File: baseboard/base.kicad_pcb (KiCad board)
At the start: 2 copper layers, 180 x 45 mm, 41 parts, among them J1 Conn_02x05_Odd_Even, J2 Barrel_Jack, J3 Barrel_Jack, J4 Conn_01x03_Male, Q1 BSS138, Q2 BSS138, Q3 BSS138, Q4 BSS138, Q5 BSS138, SW1 SW_Push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

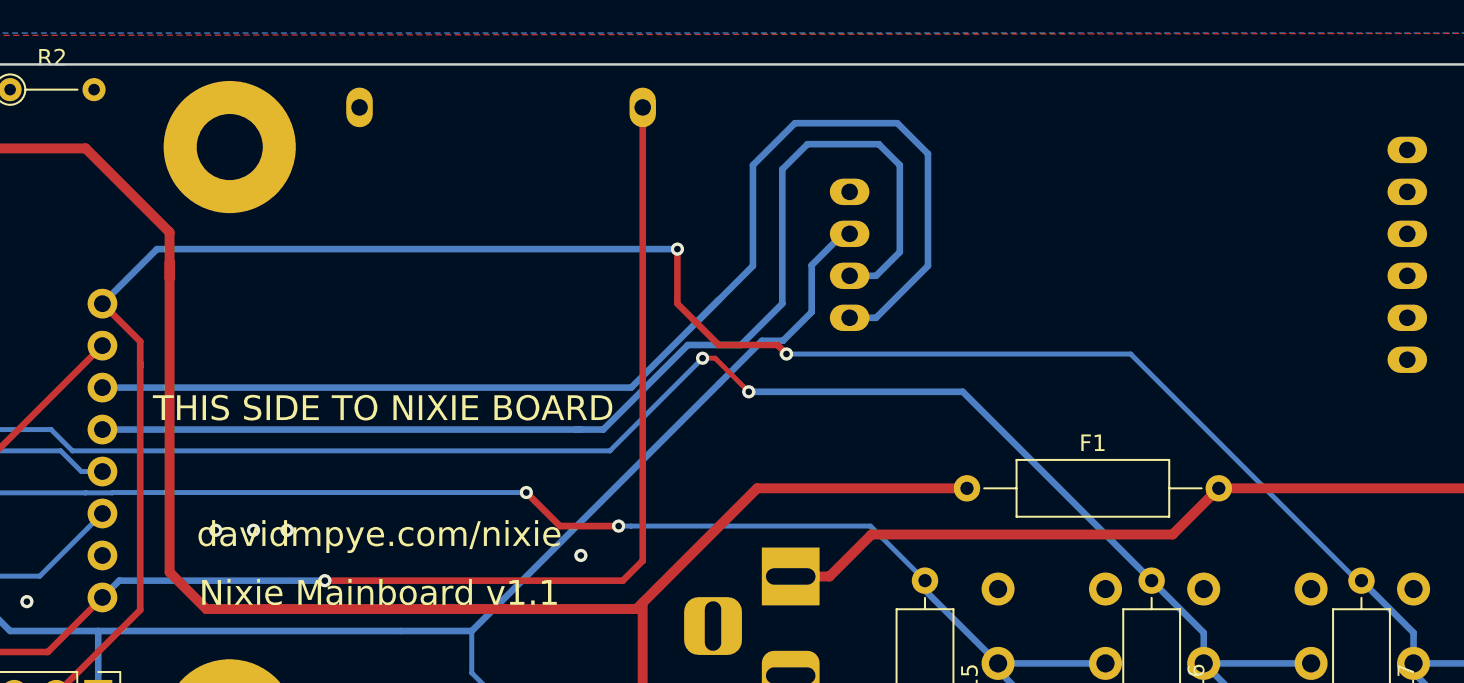
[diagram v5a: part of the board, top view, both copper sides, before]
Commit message: Track rerouting/tidying
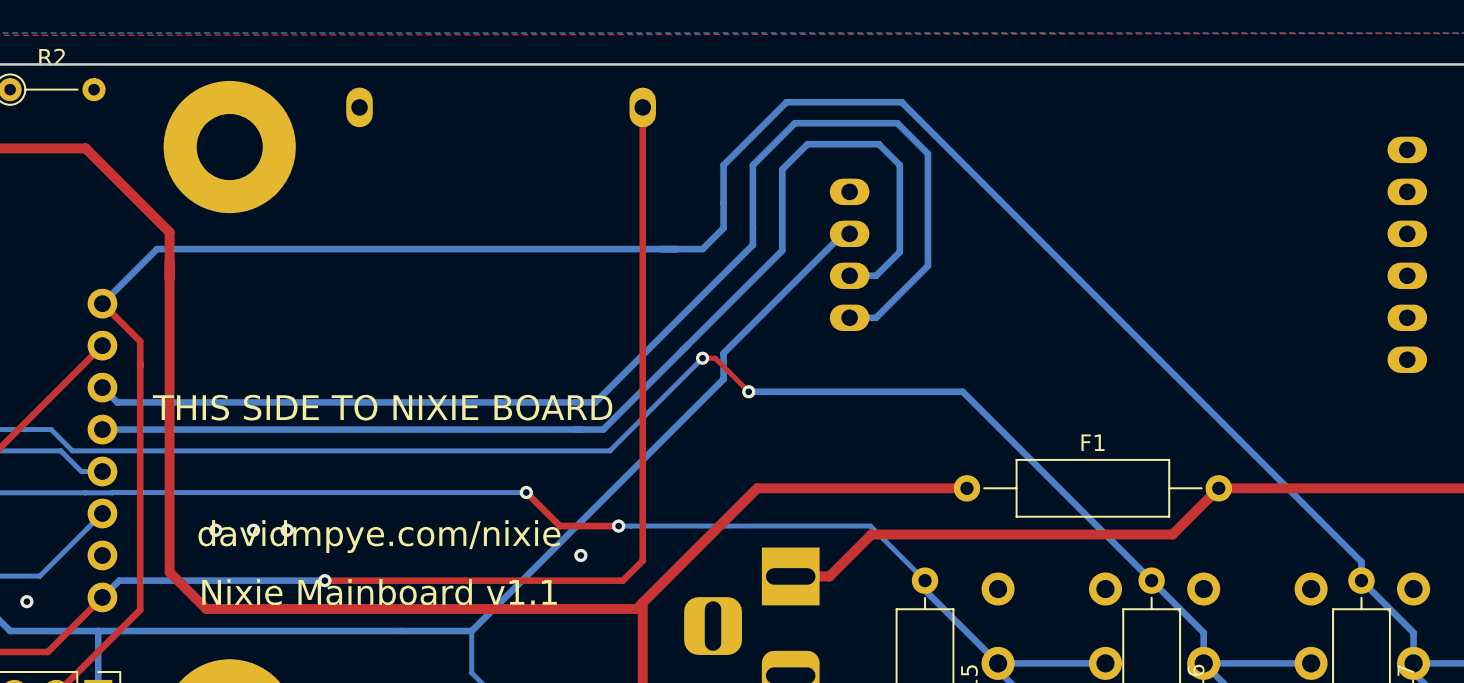
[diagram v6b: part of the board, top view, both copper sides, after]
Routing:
- net SW_3: track 137.6 -> 146.9 mm, vias 2 -> 0
- net SCL: track 75.7 -> 73.8 mm
- net SDA: track 69.8 -> 68.4 mm
- net +3V3: track 245.9 -> 245.1 mm
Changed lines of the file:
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@@
     (thickness 1.6)
     (drawings 22)
-    (tracks 367)
+    (tracks 364)
     (zones 0)
     (modules 41)
@@
   )
   (setup
-    (last_trace_width 0.25)
+    (last_trace_width 0.4)
     (user_trace_width 0.3)
     (user_trace_width 0.4)
@@
   (segment (start 101.092 65.532) (end 101.092 64.282) (width 0.4) (layer B.Cu) (net 7))
   (segment (start 123.698 61.722) (end 138.684 46.736) (width 0.4) (layer B.Cu) (net 7))
-  (segment (start 141.262001 44.157999) (end 142.532001 44.157999) (width 0.4) (layer B.Cu) (net 7))
-  (segment (start 138.684 46.736) (end 141.262001 44.157999) (width 0.4) (layer B.Cu) (net 7))
-  (segment (start 142.532001 44.157999) (end 144.272 42.418) (width 0.4) (layer B.Cu) (net 7))
-  (segment (start 144.272 39.581) (end 146.168 37.685) (width 0.4) (layer B.Cu) (net 7))
-  (segment (start 144.272 42.418) (end 144.272 39.581) (width 0.4) (layer B.Cu) (net 7))
-  (segment (start 146.568 37.685) (end 146.168 37.685) (width 0.4) (layer B.Cu) (net 7))
   (segment (start 146.568 37.685) (end 146.168 37.685) (width 0.4) (layer F.Cu) (net 7))
   (segment (start 50.8 70.866) (end 53.086 68.58) (width 0.3) (layer B.Cu) (net 7))
@@
   (segment (start 74.93 33.528) (end 74.93 40.894) (width 0.4) (layer B.Cu) (net 7))
   (segment (start 74.93 40.894) (end 74.93 43.688) (width 0.4) (layer B.Cu) (net 7))
+  (segment (start 146.168 37.685) (end 138.938 44.915) (width 0.4) (layer B.Cu) (net 7))
+  (segment (start 146.568 37.685) (end 146.168 37.685) (width 0.4) (layer B.Cu) (net 7))
+  (segment (start 138.938 44.915) (end 138.938 46.482) (width 0.4) (layer B.Cu) (net 7))
+  (segment (start 138.684 46.736) (end 138.938 46.482) (width 0.4) (layer B.Cu) (net 7))
   (segment (start 53.399 59.427) (end 53.324 59.502) (width 0.3) (layer F.Cu) (net 8))
   (segment (start 55.88 59.427) (end 53.399 59.427) (width 0.3) (layer F.Cu) (net 8))
@@
   (segment (start 101.346 49.53) (end 130.048 49.53) (width 0.4) (layer B.Cu) (net 20))
   (segment (start 130.048 49.53) (end 130.302 49.53) (width 0.4) (layer B.Cu) (net 20))
-  (segment (start 136.776543 44.411999) (end 139.992001 44.411999) (width 0.4) (layer B.Cu) (net 20))
   (segment (start 130.048 49.53) (end 131.658542 49.53) (width 0.4) (layer B.Cu) (net 20))
-  (segment (start 131.658542 49.53) (end 136.776543 44.411999) (width 0.4) (layer B.Cu) (net 20))
   (segment (start 144.018 32.258) (end 142.494 33.782) (width 0.4) (layer B.Cu) (net 20))
   (segment (start 149.606 33.528) (end 148.336 32.258) (width 0.4) (layer B.Cu) (net 20))
-  (segment (start 142.494 33.782) (end 142.494 41.91) (width 0.4) (layer B.Cu) (net 20))
   (segment (start 148.336 32.258) (end 144.018 32.258) (width 0.4) (layer B.Cu) (net 20))
-  (segment (start 139.992001 44.411999) (end 142.494 41.91) (width 0.4) (layer B.Cu) (net 20))
   (segment (start 146.568 40.225) (end 148.168 40.225) (width 0.4) (layer B.Cu) (net 20))
   (segment (start 148.168 40.225) (end 149.606 38.787) (width 0.4) (layer B.Cu) (net 20))
   (segment (start 149.606 38.787) (end 149.606 33.528) (width 0.4) (layer B.Cu) (net 20))
-  (segment (start 101.346 46.99) (end 133.35 46.99) (width 0.4) (layer B.Cu) (net 21))
+  (segment (start 142.494 38.694542) (end 136.441271 44.747271) (width 0.4) (layer B.Cu) (net 20))
+  (segment (start 142.494 33.782) (end 142.494 38.694542) (width 0.4) (layer B.Cu) (net 20))
+  (segment (start 131.658542 49.53) (end 136.441271 44.747271) (width 0.4) (layer B.Cu) (net 20))
+  (segment (start 136.441271 44.747271) (end 136.776543 44.411999) (width 0.4) (layer B.Cu) (net 20))
   (segment (start 148.168 42.765) (end 151.309 39.624) (width 0.4) (layer B.Cu) (net 21))
   (segment (start 146.568 42.765) (end 148.168 42.765) (width 0.4) (layer B.Cu) (net 21))
@@
   (segment (start 149.456 30.988) (end 143.256 30.988) (width 0.4) (layer B.Cu) (net 21))
   (segment (start 143.256 30.988) (end 140.716 33.528) (width 0.4) (layer B.Cu) (net 21))
-  (segment (start 140.716 33.528) (end 140.716 39.624) (width 0.4) (layer B.Cu) (net 21))
-  (segment (start 133.35 46.99) (end 137.287 43.053) (width 0.4) (layer B.Cu) (net 21))
-  (segment (start 140.716 39.624) (end 137.287 43.053) (width 0.4) (layer B.Cu) (net 21))
-  (segment (start 137.287 43.053) (end 138.684 41.656) (width 0.4) (layer B.Cu) (net 21))
+  (segment (start 102.245999 47.889999) (end 131.180001 47.889999) (width 0.4) (layer B.Cu) (net 21))
+  (segment (start 101.346 46.99) (end 102.245999 47.889999) (width 0.4) (layer B.Cu) (net 21))
+  (segment (start 140.716 38.354) (end 140.716 37.338) (width 0.4) (layer B.Cu) (net 21))
+  (segment (start 140.716 33.528) (end 140.716 37.338) (width 0.4) (layer B.Cu) (net 21))
+  (segment (start 131.180001 47.889999) (end 140.716 38.354) (width 0.4) (layer B.Cu) (net 21))
   (segment (start 180.19 64.184) (end 180.19 63.682) (width 0.4) (layer B.Cu) (net 22))
   (segment (start 180.19 63.682) (end 181.604213 63.682) (width 0.4) (layer B.Cu) (net 22))
-  (via (at 136.144 38.608) (size 0.8) (drill 0.4) (layers F.Cu B.Cu) (net 22))
-  (via (at 142.748 44.958) (size 0.8) (drill 0.4) (layers F.Cu B.Cu) (net 22))
-  (segment (start 163.576 44.958) (end 177.292 58.674) (width 0.3) (layer B.Cu) (net 22))
-  (segment (start 142.748 44.958) (end 163.576 44.958) (width 0.3) (layer B.Cu) (net 22))
   (segment (start 180.698 64.244) (end 180.698 63.682) (width 0.4) (layer B.Cu) (net 22))
   (segment (start 186.05 69.596) (end 180.698 64.244) (width 0.4) (layer B.Cu) (net 22))
@@
   (segment (start 180.698 61.826) (end 177.546 58.674) (width 0.4) (layer B.Cu) (net 22))
   (segment (start 180.698 63.682) (end 180.698 61.826) (width 0.4) (layer B.Cu) (net 22))
-  (segment (start 142.494 44.958) (end 142.748 44.958) (width 0.4) (layer F.Cu) (net 22))
-  (segment (start 142.201999 44.411999) (end 138.645999 44.411999) (width 0.4) (layer F.Cu) (net 22))
-  (segment (start 142.748 44.958) (end 142.201999 44.411999) (width 0.4) (layer F.Cu) (net 22))
-  (segment (start 136.144 41.91) (end 136.144 38.608) (width 0.4) (layer F.Cu) (net 22))
-  (segment (start 138.645999 44.411999) (end 136.144 41.91) (width 0.4) (layer F.Cu) (net 22))
   (segment (start 98.552 65.532) (end 103.632 60.452) (width 0.4) (layer F.Cu) (net 22))
   (segment (start 101.346 41.91) (end 103.632 44.196) (width 0.4) (layer F.Cu) (net 22))
@@
   (segment (start 104.648 38.608) (end 101.346 41.91) (width 0.4) (layer B.Cu) (net 22))
   (segment (start 136.144 38.608) (end 104.648 38.608) (width 0.4) (layer B.Cu) (net 22))
+  (segment (start 177.546 57.54263) (end 149.72137 29.718) (width 0.4) (layer B.Cu) (net 22))
+  (segment (start 177.546 58.674) (end 177.546 57.54263) (width 0.4) (layer B.Cu) (net 22))
+  (segment (start 149.72137 29.718) (end 142.748 29.718) (width 0.4) (layer B.Cu) (net 22))
+  (segment (start 142.748 29.718) (end 138.938 33.528) (width 0.4) (layer B.Cu) (net 22))
+  (segment (start 138.938 33.528) (end 138.938 35.814) (width 0.4) (layer B.Cu) (net 22))
+  (segment (start 138.938 35.814) (end 138.938 37.338) (width 0.4) (layer B.Cu) (net 22))
+  (segment (start 137.668 38.608) (end 135.128 38.608) (width 0.4) (layer B.Cu) (net 22))
+  (segment (start 138.938 37.338) (end 137.668 38.608) (width 0.4) (layer B.Cu) (net 22))
   (segment (start 57.413 42.917) (end 55.184 45.146) (width 0.4) (layer F.Cu) (net 23))
   (segment (start 58.928 42.917) (end 57.413 42.917) (width 0.4) (layer F.Cu) (net 23))
